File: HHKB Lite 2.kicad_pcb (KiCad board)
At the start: 2 copper layers, 72.4 x 48 mm, 3 parts, among them U1 Teensy2.0_(C)

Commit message: Add Molex Easy-On connector footprints
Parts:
- J_Col1: footprint Connector_FFC-FPC:Molex_Easy-On_39-53-2144_14-Contacts -> Connector_Molex_Easy-On:Molex_Easy-On_39-53-2144_14-Contacts
- J_Row1: footprint Connector_FFC-FPC:Molex_Easy-On_39-53-2084_8-Contacts -> Connector_Molex_Easy-On:Molex_Easy-On_39-53-2084_8-Contacts
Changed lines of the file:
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@@
     (add_net "Net-(U1-Pad15)")
   )
-  (module Connector_FFC-FPC:Molex_Easy-On_39-53-2084_8-Contacts (layer F.Cu)
+  (module Connector_Molex_Easy-On:Molex_Easy-On_39-53-2084_8-Contacts (layer F.Cu)
     (at 134.112 75.438 180)
     (fp_text reference J_Row1 (at 4.318 4.064) (layer F.SilkS)
@@
       (net 22 "Net-(J_Row1-Pad1)"))
   )
-  (module Connector_FFC-FPC:Molex_Easy-On_39-53-2144_14-Contacts (layer F.Cu)
+  (module Connector_Molex_Easy-On:Molex_Easy-On_39-53-2144_14-Contacts (layer F.Cu)
     (at 169.91 73.152)
     (fp_text reference J_Col1 (at 8.144 -3.048) (layer F.SilkS)

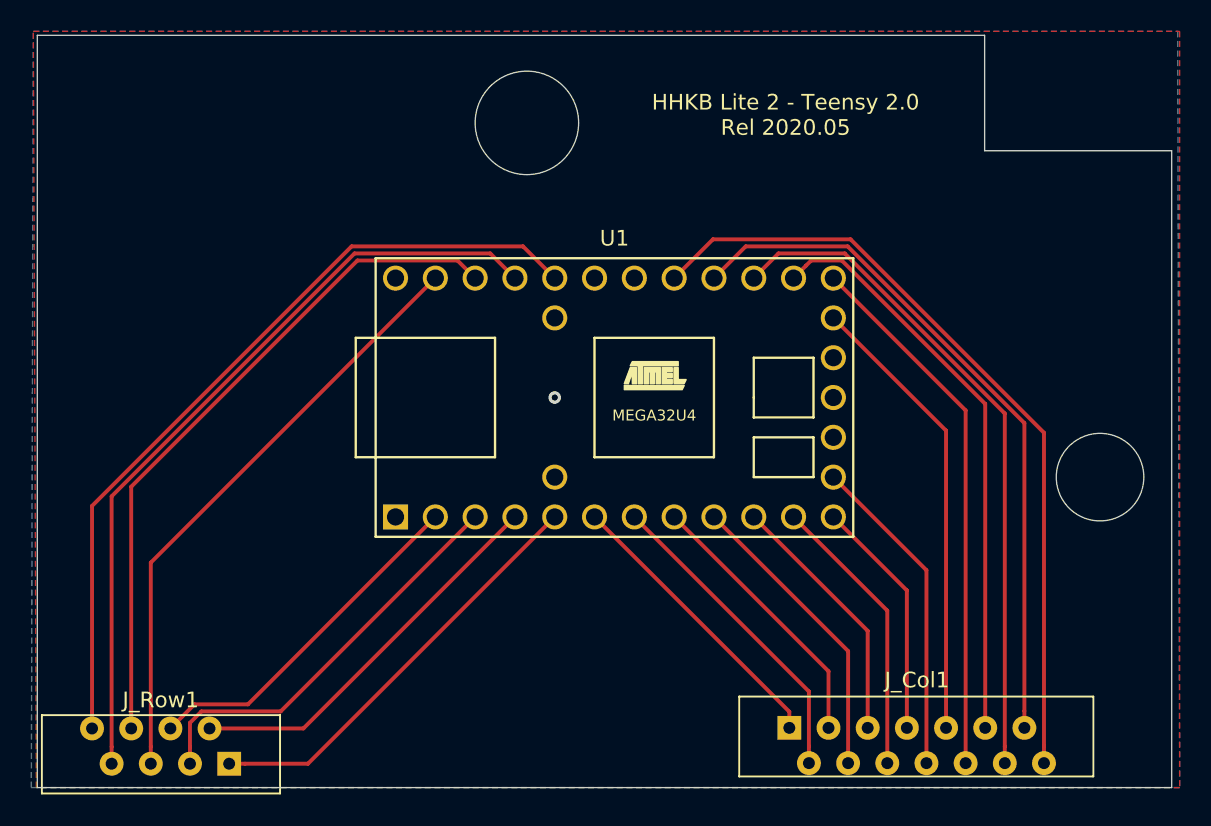
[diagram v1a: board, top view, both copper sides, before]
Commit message: Flip Teensy
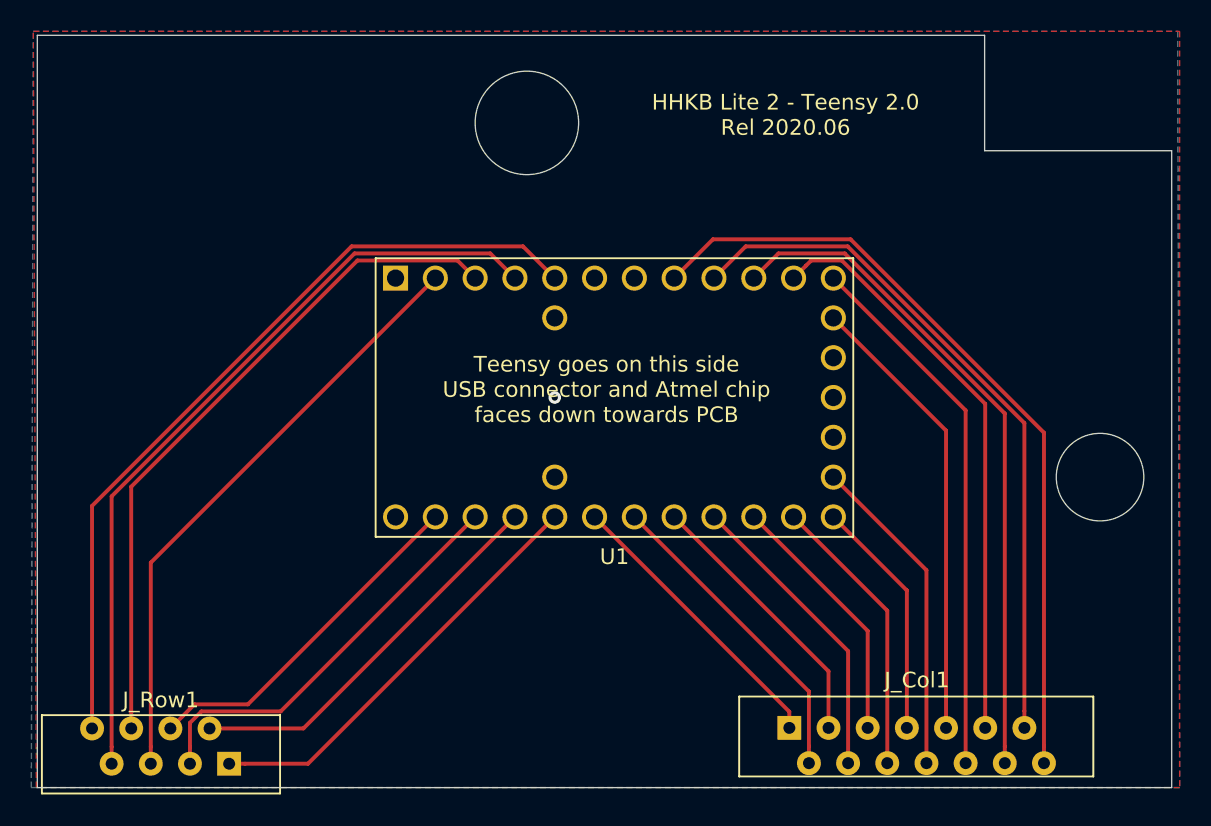
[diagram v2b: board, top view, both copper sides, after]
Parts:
- U1: moved to B.Cu
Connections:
- U1 pad 10: Net-(J_Col1-Pad5) -> Net-(J_Col1-Pad12)
- U1 pad 11: Net-(J_Col1-Pad6) -> Net-(J_Col1-Pad11)
- U1 pad 12: Net-(J_Col1-Pad7) -> Net-(J_Col1-Pad10)
- U1 pad 13: Net-(J_Col1-Pad8) -> Net-(J_Col1-Pad9)
- U1 pad 17: Net-(J_Col1-Pad9) -> Net-(J_Col1-Pad8)
- U1 pad 18: Net-(J_Col1-Pad10) -> Net-(J_Col1-Pad7)
- U1 pad 19: Net-(J_Col1-Pad11) -> Net-(J_Col1-Pad6)
- U1 pad 2: Net-(J_Row1-Pad4) -> Net-(J_Row1-Pad5)
- U1 pad 20: Net-(J_Col1-Pad12) -> Net-(J_Col1-Pad5)
- U1 pad 21: Net-(J_Col1-Pad13) -> Net-(J_Col1-Pad4)
- U1 pad 22: Net-(J_Col1-Pad14) -> Net-(J_Col1-Pad3)
- U1 pad 23: (no net) -> Net-(J_Col1-Pad2)
- U1 pad 24: (no net) -> Net-(J_Col1-Pad1)
- U1 pad 25: Net-(J_Row1-Pad8) -> Net-(J_Row1-Pad1)
- U1 pad 26: Net-(J_Row1-Pad7) -> Net-(J_Row1-Pad2)
- U1 pad 27: Net-(J_Row1-Pad6) -> Net-(J_Row1-Pad3)
- U1 pad 28: Net-(J_Row1-Pad5) -> Net-(J_Row1-Pad4)
- U1 pad 3: Net-(J_Row1-Pad3) -> Net-(J_Row1-Pad6)
- U1 pad 4: Net-(J_Row1-Pad2) -> Net-(J_Row1-Pad7)
- U1 pad 5: Net-(J_Row1-Pad1) -> Net-(J_Row1-Pad8)
- U1 pad 6: Net-(J_Col1-Pad1) -> (no net)
- U1 pad 7: Net-(J_Col1-Pad2) -> (no net)
- U1 pad 8: Net-(J_Col1-Pad3) -> Net-(J_Col1-Pad14)
- U1 pad 9: Net-(J_Col1-Pad4) -> Net-(J_Col1-Pad13)
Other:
- board text added: "DO NOT MOUNT HERE"
- board text added: "HHKB Lite 2 - Teensy 2.0 Rel 2020.06"
- board text added: "Teensy goes on this side USB connector and Atmel chip faces down towards PCB"
- board text removed: "HHKB Lite 2 - Teensy 2.0 Rel 2020.05"
